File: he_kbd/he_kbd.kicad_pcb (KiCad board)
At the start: 2 copper layers, 162.2 x 126.5 mm, 270 parts, among them J1 AudioJack4, J2 Conn_01x08_Pin, J3 AudioJack4, J4 Conn_01x08_Pin

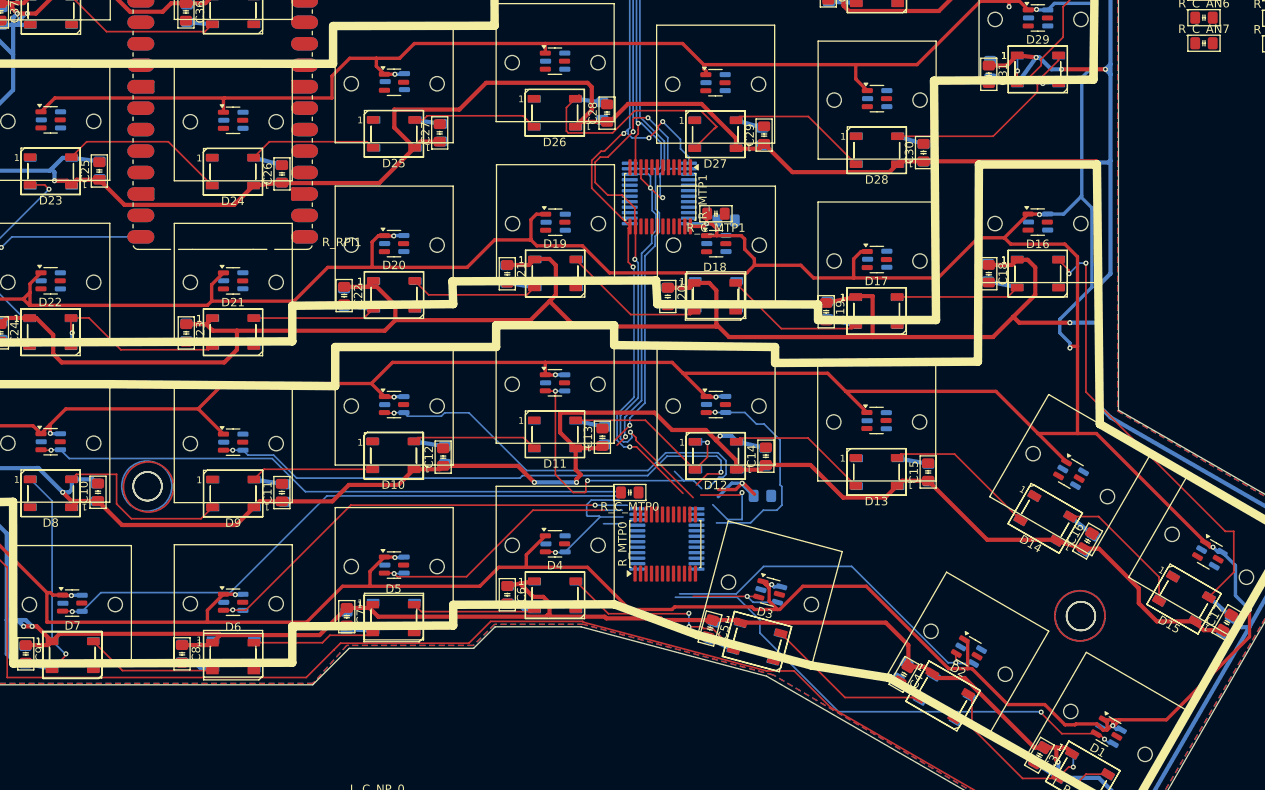
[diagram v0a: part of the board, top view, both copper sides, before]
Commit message: changed track width for analog sig to .1mm
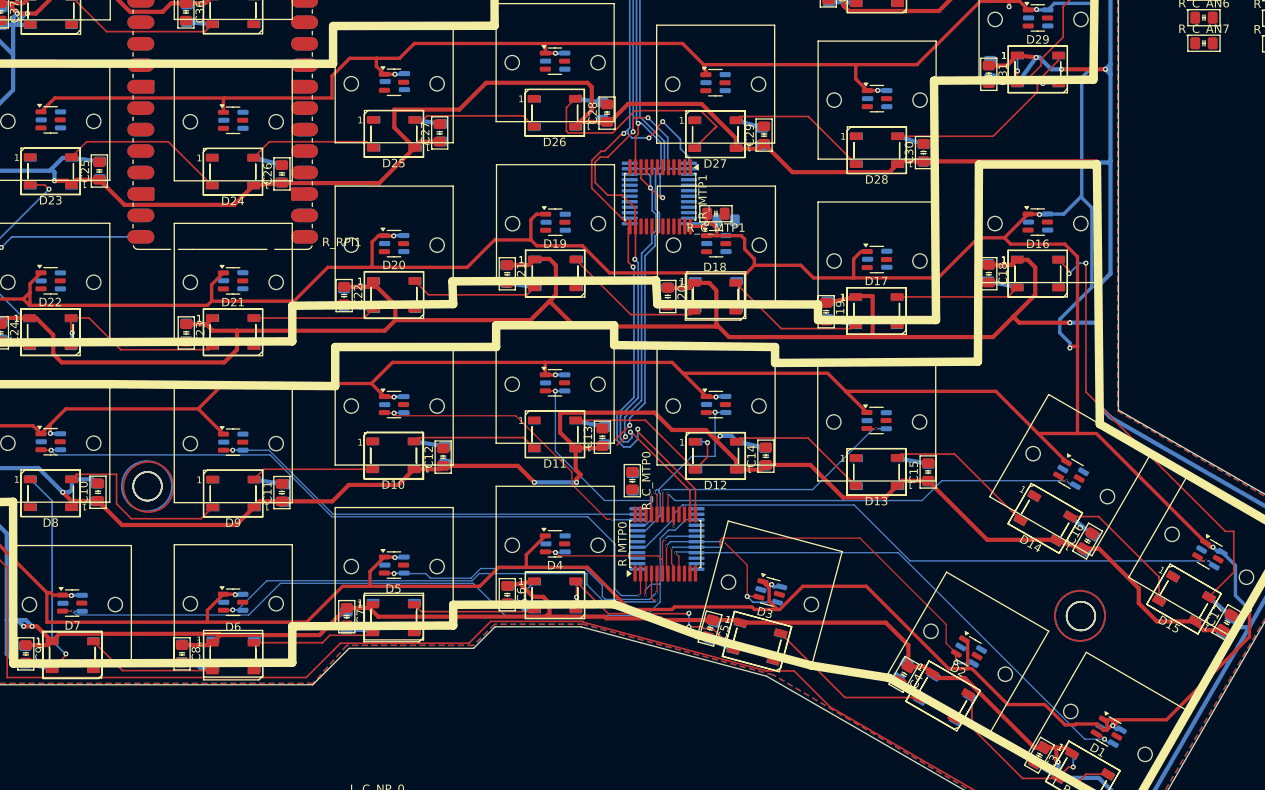
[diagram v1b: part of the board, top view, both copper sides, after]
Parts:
- moved L_C_MTP0 15.4 mm to (97.4, 111.2), turned to -90 degrees
- moved R_C_MTP0 1.43 mm to (97.4, 111.1), turned to -90 degrees
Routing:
- net /hesig15: track 0.00 -> 77.2 mm, vias 0 -> 2
- net /hesig14: track 0.00 -> 53.5 mm, vias 0 -> 2
- net /hesig13: track 0.00 -> 33.4 mm, vias 0 -> 2
- net /hesig9: track 78.9 -> 53.4 mm, vias 3 -> 1
- net /hesig7: track 71.9 -> 93.9 mm, vias 1 -> 2
- net /hesig8: track 70.4 -> 84.9 mm, vias 1 -> 2
- net /hesig10: track 49.5 -> 37.3 mm, vias 1 -> 2
- net /hesig3: track 13.8 -> 23.2 mm, vias 1 -> 3
- net /hesig4: track 18.0 -> 25.1 mm, vias 1 -> 2
- net /MTP_BIN_3: track 135.5 -> 142.3 mm
- net /hesig5: track 32.8 -> 39.0 mm, vias 1 -> 2
- net /hesig2: track 42.0 -> 48.2 mm, vias 1 -> 3
- net /3V3: track 1106.5 -> 1100.5 mm, vias 29 -> 30
- net /hesig6: track 54.2 -> 60.1 mm
- net /hesig1: track 60.0 -> 65.2 mm
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
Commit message: mtp0 done ?!
mostly done at least, probably still some stuff to do
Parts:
- moved L_C_MTP0 0.70 mm to (96.7, 111.2)
- moved R_C_MTP0 0.60 mm to (96.8, 111.1)
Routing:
- net /hesig16: track 0.00 -> 72.0 mm, vias 0 -> 4
- net /ADC_0: track 0.00 -> 34.1 mm, vias 0 -> 3
- net /MTP_BIN_0: track 126.3 -> 154.7 mm, vias 5 -> 6
- net /MTP_BIN_1: track 121.8 -> 146.1 mm, vias 4 -> 6
- net /hesig5: track 39.0 -> 63.3 mm, vias 2 -> 3
- net /3V3: track 1100.5 -> 1120.7 mm, vias 30 -> 33
- net /MTP_BIN_2: track 144.2 -> 164.1 mm, vias 8 -> 9
- net /MTP_BIN_3: track 142.3 -> 161.5 mm
- net /hesig8: track 84.9 -> 96.4 mm
- net /hesig10: track 37.3 -> 47.7 mm, vias 2 -> 5
- net /hesig6: track 60.1 -> 69.4 mm, vias 2 -> 3
- net /hesig14: track 53.5 -> 62.6 mm, vias 2 -> 3
- net /hesig9: track 53.4 -> 59.5 mm, vias 1 -> 4
- net /hesig13: track 33.4 -> 38.3 mm, vias 2 -> 3
- net /hesig4: track 25.1 -> 29.6 mm, vias 2 -> 5
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
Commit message: mtp1 almost finished!!
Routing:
- net /ADC_0: track 34.1 -> 128.7 mm, vias 3 -> 4
- net /hesig22: track 0.00 -> 90.0 mm, vias 0 -> 8
- net /ADC_1: track 0.00 -> 73.9 mm, vias 0 -> 2
- net /hesig24: track 0.00 -> 69.5 mm, vias 0 -> 7
- net /hesig29: track 0.00 -> 66.1 mm, vias 0 -> 2
- net /hesig25: track 0.00 -> 54.9 mm, vias 0 -> 4
- net /hesig31: track 0.00 -> 54.8 mm, vias 0 -> 2
- net /hesig30: track 0.00 -> 54.4 mm, vias 0 -> 2
- net /hesig32: track 0.00 -> 53.8 mm, vias 0 -> 4
- net /hesig20: track 0.00 -> 40.5 mm, vias 0 -> 2
- net /hesig28: track 0.00 -> 38.1 mm, vias 0 -> 2
- net /hesig26: track 0.00 -> 33.6 mm, vias 0 -> 3
- net /hesig27: track 0.00 -> 22.2 mm, vias 0 -> 4
- net /hesig23: track 0.00 -> 19.8 mm, vias 0 -> 3
- net /hesig19: track 0.00 -> 17.3 mm, vias 0 -> 2
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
